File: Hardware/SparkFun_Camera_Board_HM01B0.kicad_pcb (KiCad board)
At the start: 4 copper layers, 22.9 x 35.6 mm, 112 parts, among them J1 Conn_01x09, J2 Conn_01x09, J3 Conn_01x09, J4 HM01B0, Q1 RE1C002UNTCL, Q2 RE1C002UNTCL, Q3 RE1C002UNTCL, Q4 RE1C002UNTCL, U1 HM01B0, U2 RT9080-1.2V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

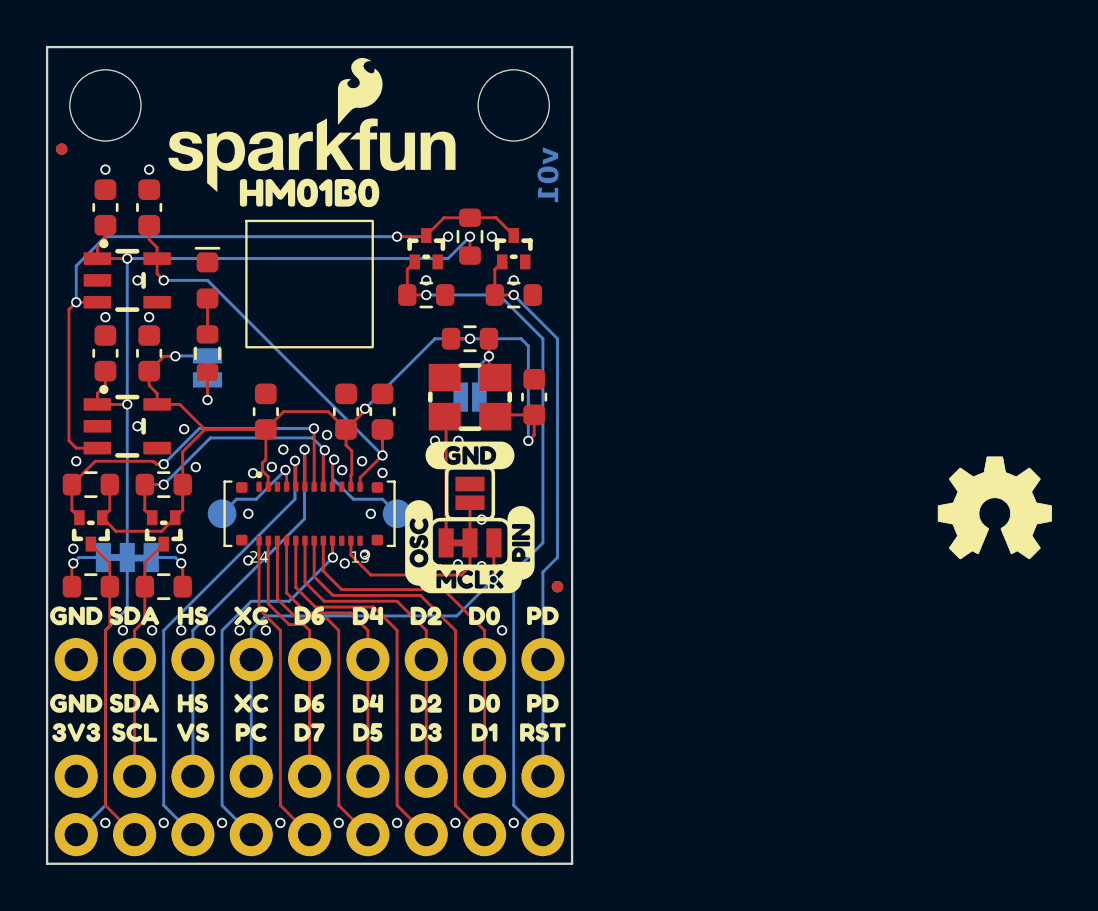
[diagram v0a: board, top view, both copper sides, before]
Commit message: Silkscreen tweaks
Move OSHW logo to back
Add PWR label to power LED
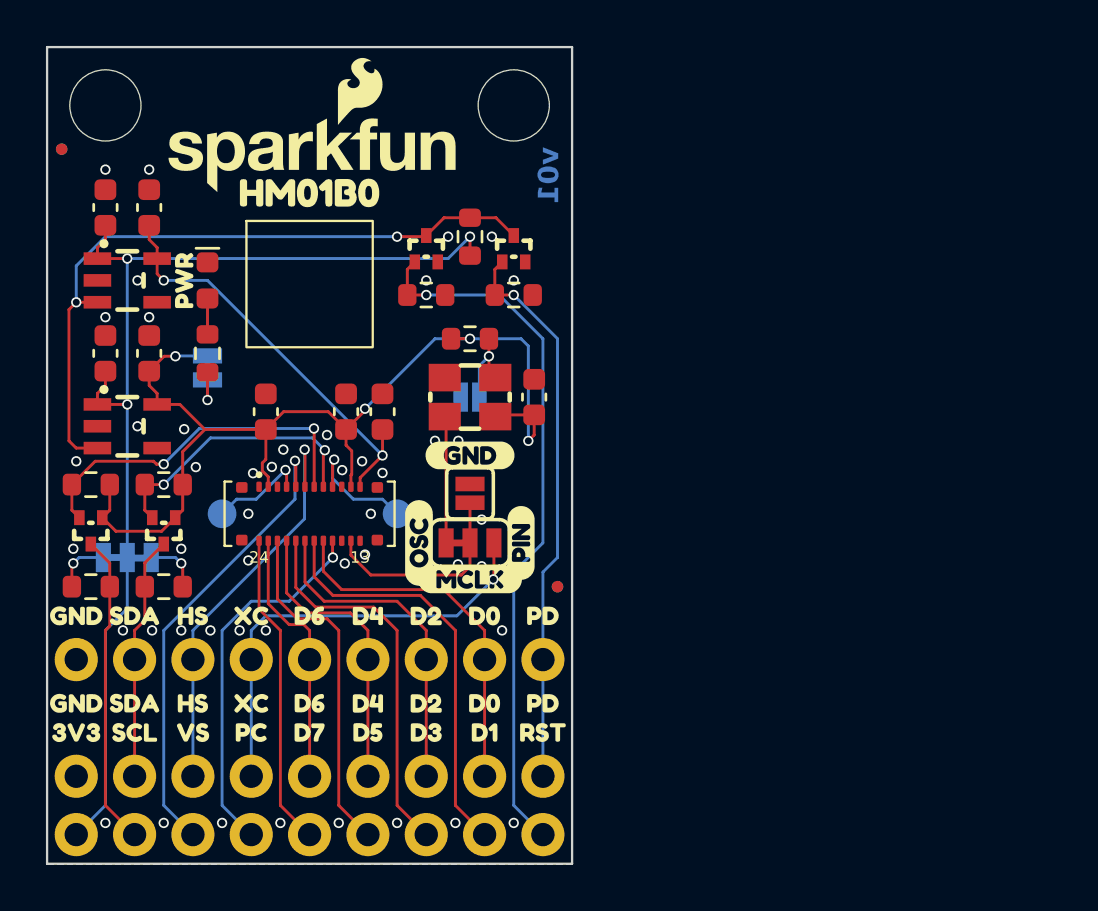
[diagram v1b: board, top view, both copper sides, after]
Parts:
- added kibuzzard-67D21B41: G***, kibuzzard-67D21B41, F.Cu at (121.5, 99.1)
- Ref**: moved to B.Cu
- moved Ref** 22.3 mm to (134.6, 110.5), turned to 180 degrees

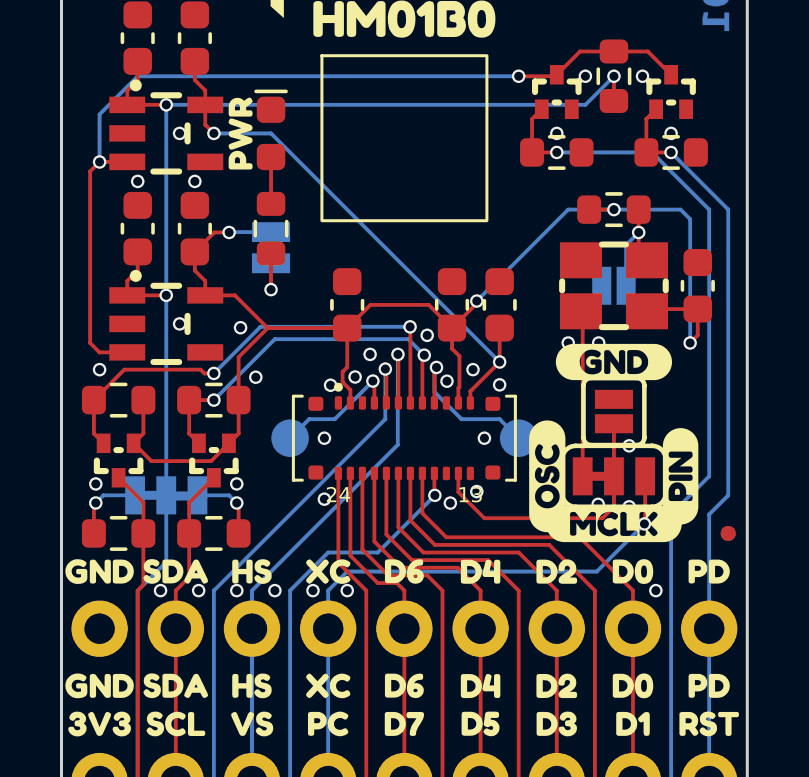
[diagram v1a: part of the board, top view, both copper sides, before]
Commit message: Design review updates
Rearrange power control circuitry in schematic
Add note to MCLK jumper in schematic
Change camera connector silk pin labels
Improve GND continuity
Increase thermal spoke width
Change In2.Cu to 2.8V instead of GND
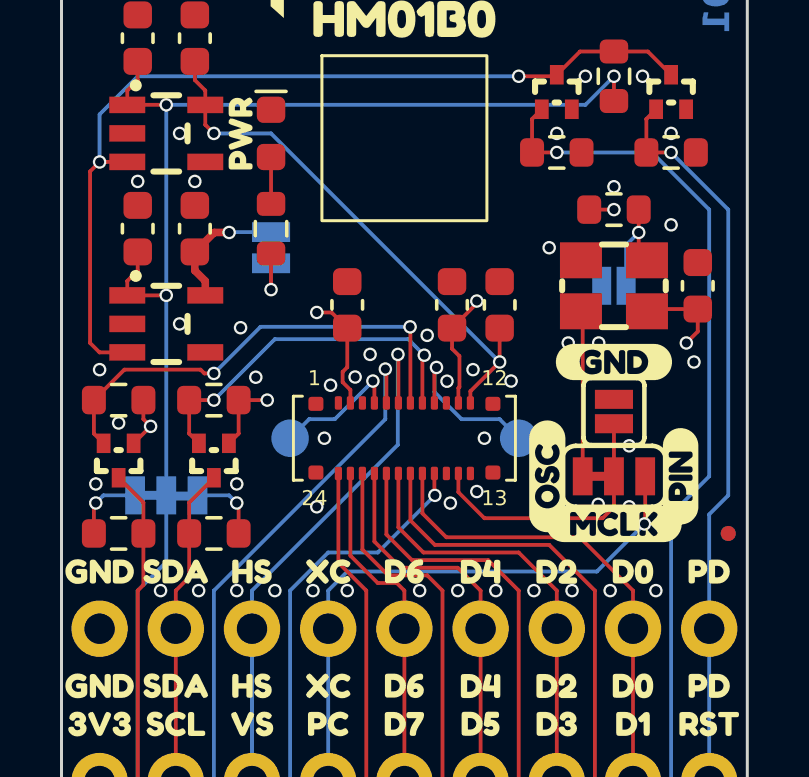
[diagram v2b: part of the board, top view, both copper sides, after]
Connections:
- net EN renamed Net-(Q3-D)
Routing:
- net 2.8V: track 46.3 -> 20.3 mm, vias 4 -> 7
- net GND: vias 47 -> 58
- added copper zone on In2.Cu, net 2.8V
- removed copper zone on In2.Cu, net GND

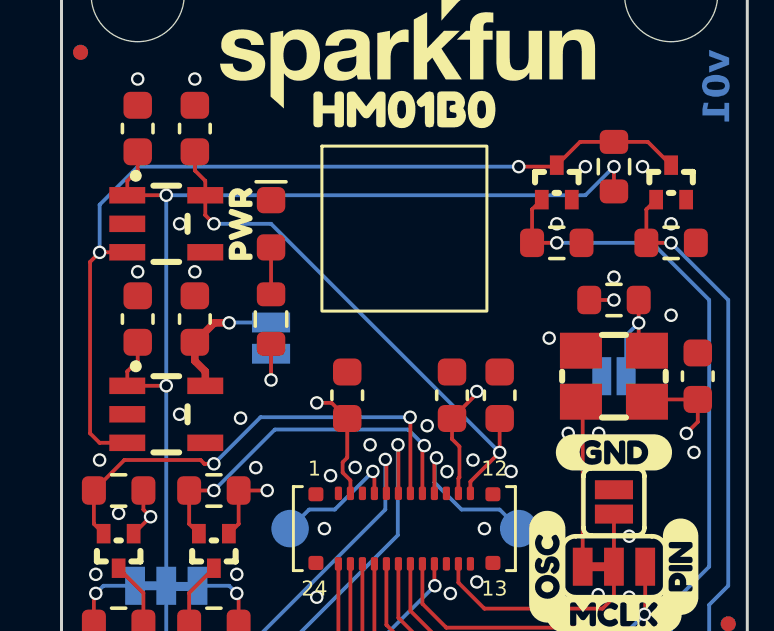
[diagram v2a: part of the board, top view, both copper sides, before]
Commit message: Change regulators to adjustable type
Using adjustable regulators at least for prototypes. May change back to fixed regulators depending on testing
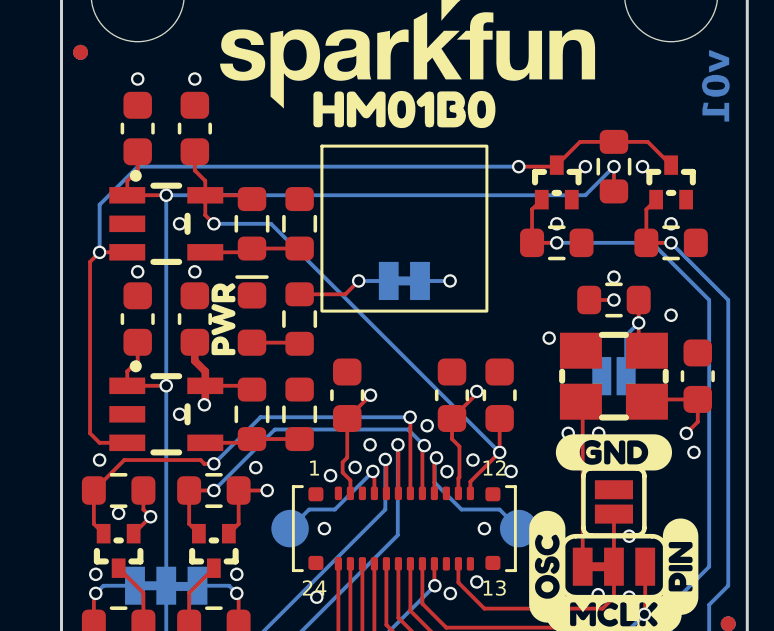
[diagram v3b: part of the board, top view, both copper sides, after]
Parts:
- added R10: 22k, SparkFun-Resistor:R_0603_1608Metric, F.Cu at (121.9, 99.1)
- added R11: 100k, SparkFun-Resistor:R_0603_1608Metric, F.Cu at (123.5, 99.1)
- added R12: 200k, SparkFun-Resistor:R_0603_1608Metric, F.Cu at (121.9, 105.4)
- added R13: 150k, SparkFun-Resistor:R_0603_1608Metric, F.Cu at (123.5, 105.4)
- U2: value RT9080-1.2V -> MIC5205
- U3: value RT9080-2.8V -> MIC5205
- moved JP7 4.84 mm to (127.0, 101.0), turned to 0 degrees
- moved kibuzzard-67C103CA 4.76 mm to (127.0, 99.4)
- moved D1 3.24 mm to (121.9, 102.2)
- moved kibuzzard-67D21B41 3.23 mm to (121.0, 102.2)
- moved R7 0.95 mm to (123.5, 102.2), turned to 90 degrees
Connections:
- U2 pad 4: unconnected-(U2-NC-Pad4) -> Net-(U2-ADJ)
- U3 pad 4: unconnected-(U3-NC-Pad4) -> Net-(U3-ADJ)
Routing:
- net Net-(U3-ADJ): track 0.00 -> 3.20 mm
- net Net-(U2-ADJ): track 0.00 -> 3.20 mm
- net 1.5V: track 18.2 -> 19.9 mm
- net Net-(JP7-A): track 2.08 -> 3.16 mm
- net 2.8V: track 20.3 -> 20.6 mm, vias 7 -> 8
- net GND: vias 58 -> 57

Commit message: Fix voltage regulator resistor orders
Reference voltage is relative to VOUT instead  of GND. Why???
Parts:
- R10: value 22k -> 100k
- R11: value 100k -> 22k
- R12: value 200k -> 150k
- R13: value 150k -> 200k
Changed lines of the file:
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@@
 			)
 		)
-		(property "Value" "200k"
+		(property "Value" "150k"
 			(at 0 1.43 90)
 			(layer "F.Fab")
@@
 			)
 		)
-		(property "PROD_ID" "RES-09385"
+		(property "PROD_ID" "RES-09117"
 			(at 0 0 90)
 			(unlocked yes)
@@
 			)
 		)
-		(property "Value" "150k"
+		(property "Value" "200k"
 			(at 0 1.43 90)
 			(layer "F.Fab")
@@
 			)
 		)
-		(property "PROD_ID" "RES-09117"
+		(property "PROD_ID" "RES-09385"
 			(at 0 0 -90)
 			(unlocked yes)
@@
 			)
 		)
-		(property "Value" "100k"
+		(property "Value" "22k"
 			(at 0 1.43 90)
 			(layer "F.Fab")
@@
 			)
 		)
-		(property "PROD_ID" "RES-07828"
+		(property "PROD_ID" "RES-07853"
 			(at 0 0 -90)
 			(unlocked yes)
@@
 			)
 		)
-		(property "Value" "22k"
+		(property "Value" "100k"
 			(at 0 1.43 90)
 			(layer "F.Fab")
@@
 			)
 		)
-		(property "PROD_ID" "RES-07853"
+		(property "PROD_ID" "RES-07828"
 			(at 0 0 90)
 			(unlocked yes)

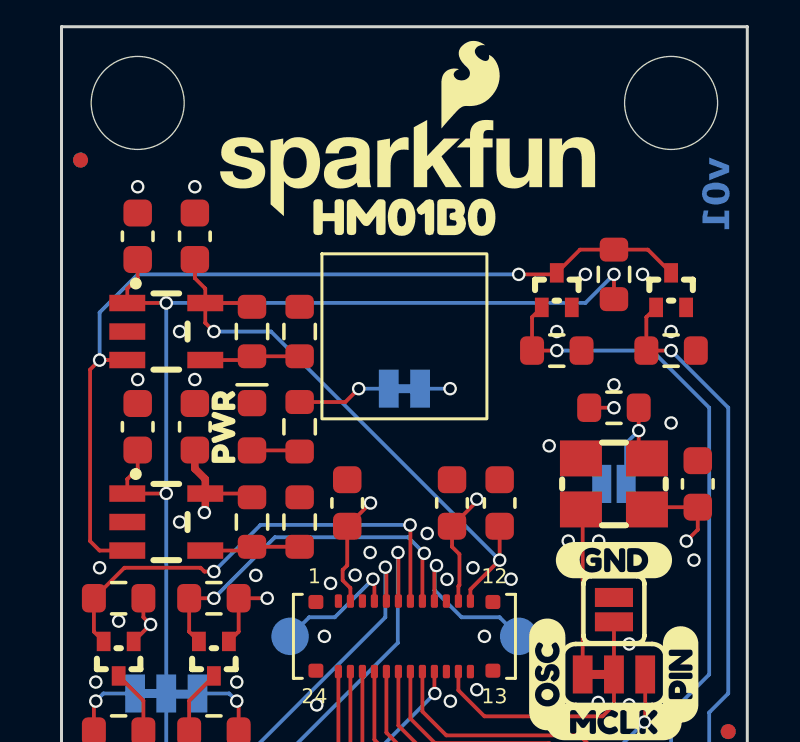
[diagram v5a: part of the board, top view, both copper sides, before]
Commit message: Update voltage regulaotrs
Remove 1.5V regulator (HM01B0 has internal 1.5V LDO)
Change 2.8V regulator to RT9080 (much lower quiescent current and ripple than MIC5205)
Add test points for 1.5V and 2.8V rails
Adjust power LED position
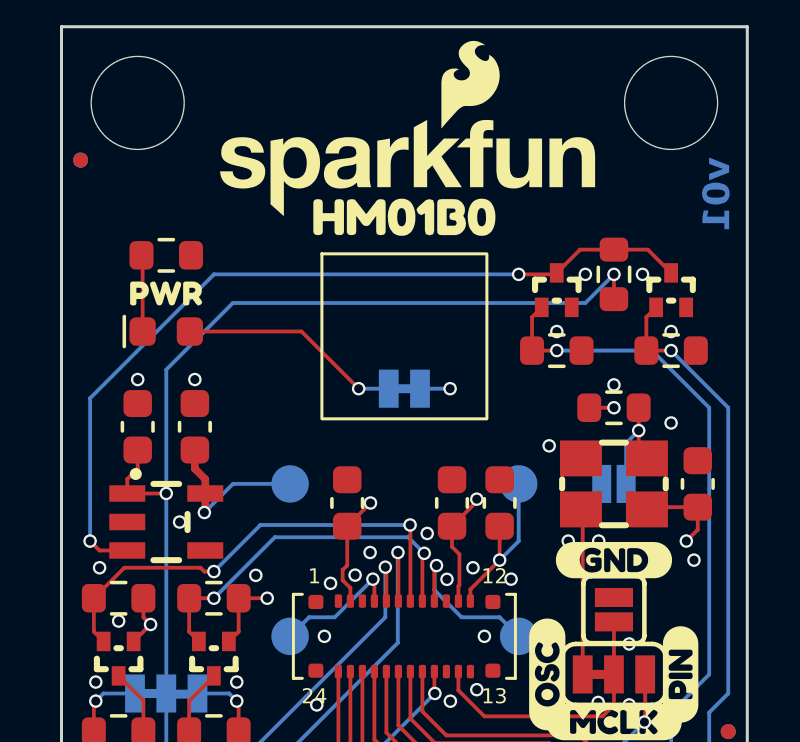
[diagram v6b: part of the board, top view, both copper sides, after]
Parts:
- removed C3, C4: 2.2uF, SparkFun-Capacitor:C_0603_1608Metric
- removed R10: 100k, SparkFun-Resistor:R_0603_1608Metric
- removed R11: 22k, SparkFun-Resistor:R_0603_1608Metric
- removed R12: 150k, SparkFun-Resistor:R_0603_1608Metric
- removed R13: 200k, SparkFun-Resistor:R_0603_1608Metric
- removed U3: MIC5205, SparkFun-Semiconductor-Standard:SOT23-5
- added TP3: 1.25mm, SparkFun-Connector:TestPoint-1.25mm, B.Cu at (123.2, 104.1)
- added TP4: 1.25mm, SparkFun-Connector:TestPoint-1.25mm, B.Cu at (130.8, 104.1)
- added kibuzzard-681BB1E7: G***, kibuzzard-681BB1E7, B.Cu at (130.8, 105.4)
- added kibuzzard-681BB1F9: G***, kibuzzard-681BB1F9, B.Cu at (123.2, 105.4)
- U2: value MIC5205 -> RT9080-2.8V
- moved TP1 7.62 mm to (123.2, 109.2)
- moved TP2 7.62 mm to (130.8, 109.2)
- moved R7 7.24 mm to (119.1, 96.5), turned to 180 degrees
- moved C1 6.35 mm to (118.1, 102.2)
- moved U2 6.35 mm to (119.1, 105.4)
- moved kibuzzard-67D21B41 4.84 mm to (119.1, 97.8), turned to 0 degrees
- moved D1 4.27 mm to (119.1, 99.1), turned to 0 degrees
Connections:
- D1 pad 1: GND -> Net-(D1-K)
- JP7 pad 1: Net-(JP7-A) -> Net-(D1-A)
- R7 pad 1: Net-(D1-A) -> GND
- R7 pad 2: Net-(JP7-A) -> Net-(D1-K)
- TP1 pad 1: Net-(J4-INT) -> Net-(J4-TRIG)
- TP2 pad 1: Net-(J4-TRIG) -> Net-(J4-INT)
- U2 pad 4: Net-(U2-ADJ) -> unconnected-(U2-NC-Pad4)
- U2 pad 5: 1.5V -> 2.8V
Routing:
- net 1.5V: track 19.9 -> 5.70 mm, vias 2 -> 1
- net Net-(D1-A): track 1.60 -> 7.42 mm, vias 0 -> 1
- net 3.3V: track 47.9 -> 43.7 mm, vias 3 -> 2
- net Net-(U3-ADJ): track 3.20 -> 0.00 mm
- net Net-(U2-ADJ): track 3.20 -> 0.00 mm
- net Net-(JP7-A): track 3.16 -> 0.00 mm, vias 1 -> 0
- net Net-(D1-K): track 0.00 -> 2.56 mm
- net Net-(Q3-D): track 30.3 -> 27.9 mm
- net 2.8V: track 20.6 -> 22.3 mm
- net GND: vias 57 -> 54

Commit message: Bump version number to v10
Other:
- board text added: "v10"
- board text removed: "v01"
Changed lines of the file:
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@@
 	(title_block
 		(title "SparkFun Camera Board - HM01B0")
-		(date "2025-03-12")
-		(rev "v01")
+		(date "2025-05-07")
+		(rev "v10")
 		(company "SparkFun Electronics")
 		(comment 1 "Designed by: Dryw Wade")
@@
 		(tags "SparkFun resistor")
 		(property "Reference" "R7"
-			(at 0 -1.43 360)
+			(at 0 -1.43 0)
 			(layer "F.Fab")
 			(effects
@@
 		)
 		(property "Value" "2.2k"
-			(at 0 1.43 360)
+			(at 0 1.43 0)
 			(layer "F.Fab")
 			(effects
@@
 		(tags "kb_params=eyJBbGlnbm1lbnRDaG9pY2UiOiAiTGVmdCIsICJDYXBMZWZ0Q2hvaWNlIjogIiIsICJDYXBSaWdodENob2ljZSI6ICIiLCAiRm9udENvbWJvQm94IjogIkZyZWRkeVNwYXJrLVJlZ3VsYXIiLCAiSGVpZ2h0Q3RybCI6IDAuOCwgIkxheWVyQ29tYm9Cb3giOiAiRi5TaWxrUyIsICJMaW5lU3BhY2luZ0N0cmwiOiAxLjUsICJNdWx0aUxpbmVUZXh0IjogIlBXUiIsICJQYWRkaW5nQm90dG9tQ3RybCI6IDIuMCwgIlBhZGRpbmdMZWZ0Q3RybCI6IDIuMCwgIlBhZGRpbmdSaWdodEN0cmwiOiAyLjAsICJQYWRkaW5nVG9wQ3RybCI6IDIuMCwgIldpZHRoQ3RybCI6IDAuMCwgImFkdmFuY2VkQ2hlY2tib3giOiBmYWxzZSwgImlubGluZUZvcm1hdFRleHRib3giOiBmYWxzZSwgImxpbmVvdmVyU3R5bGVDaG9pY2UiOiAiU3F1YXJlIiwgImxpbmVvdmVyVGhpY2tuZXNzQ3RybCI6IDF9")
 		(property "Reference" "kibuzzard-67D21B41"
-			(at 0 -3.459445 360)
+			(at 0 -3.459445 0)
 			(layer "F.SilkS")
 			(hide yes)
@@
 		)
 		(property "Value" "G***"
-			(at 0 3.459445 360)
+			(at 0 3.459445 0)
 			(layer "F.SilkS")
 			(hide yes)
@@
 		)
 		(property "Footprint" ""
-			(at 0 0 360)
+			(at 0 0 0)
 			(layer "F.Fab")
 			(hide yes)
@@
 		)
 		(property "Datasheet" ""
-			(at 0 0 360)
+			(at 0 0 0)
 			(layer "F.Fab")
 			(hide yes)
@@
 		)
 		(property "Description" ""
-			(at 0 0 360)
+			(at 0 0 0)
 			(layer "F.Fab")
 			(hide yes)
@@
 		(tags "SparkFun LED")
 		(property "Reference" "D1"
-			(at 0 -1.43 360)
+			(at 0 -1.43 0)
 			(layer "F.Fab")
 			(effects
@@
 		)
 		(property "Value" "Red"
-			(at 0 1.43 360)
+			(at 0 1.43 0)
 			(layer "F.Fab")
 			(effects
@@
 				(font
 					(size 0.001 0.001)
+					(thickness 0.15)
 				)
 				(justify mirror)
@@
 				(font
 					(size 0.001 0.001)
+					(thickness 0.15)
 				)
 				(justify mirror)
@@
 				(font
 					(size 0.001 0.001)
+					(thickness 0.15)
 				)
 				(justify mirror)
@@
 				(font
 					(size 0.001 0.001)
+					(thickness 0.15)
 				)
 				(justify mirror)
@@
 		(layer "Edge.Cuts")
 	)
-	(gr_text "v01"
+	(gr_text "v10"
 		(at 137.414 94.488 90)
 		(layer "B.Cu" knockout)

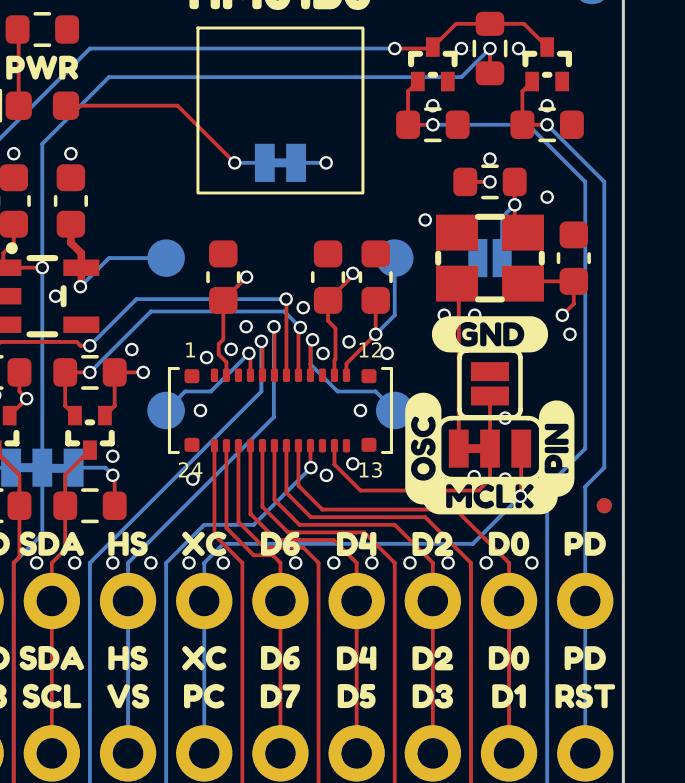
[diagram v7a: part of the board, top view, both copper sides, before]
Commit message: Design review updates
Rename OSC jumper to OSC_DIS
Add default text to MCLK jumper table
Clarify MCLK PTH Pad in MCLK jumper table
Fix typo in MCLK jumper table
Fix LED datasheet
Change MCLK pad silk labels to non-inverted
Add GND via to fix GND peninsula on side of board
Remove GND vias creating islands between data pins
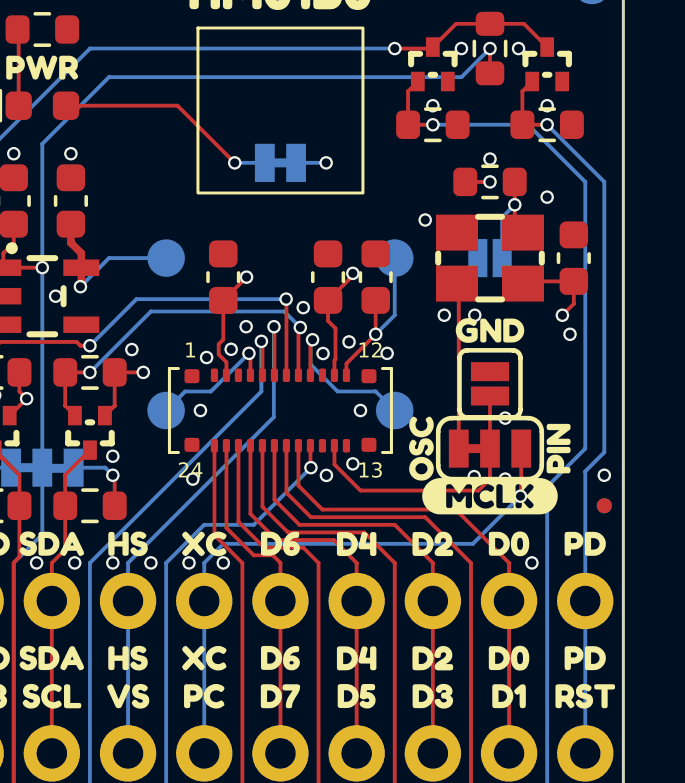
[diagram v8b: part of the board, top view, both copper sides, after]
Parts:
- removed kibuzzard-67BD0D0F: G***, kibuzzard-67BD0D0F
- removed kibuzzard-67BD0E1B: G***, kibuzzard-67BD0E1B
- removed kibuzzard-67BD0E24: G***, kibuzzard-67BD0E24
- removed kibuzzard-67BD0E2D: G***, kibuzzard-67BD0E2D
- added kibuzzard-681E4621: G***, kibuzzard-681E4621, B.Cu at (134.0, 102.6)
- added kibuzzard-681E464E: G***, kibuzzard-681E464E, F.Cu at (131.7, 110.5)
- added kibuzzard-681E4657: G***, kibuzzard-681E4657, F.Cu at (136.3, 110.5)
- added kibuzzard-681E465E: G***, kibuzzard-681E465E, F.Cu at (134.0, 106.6)
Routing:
- net GND: vias 54 -> 49
